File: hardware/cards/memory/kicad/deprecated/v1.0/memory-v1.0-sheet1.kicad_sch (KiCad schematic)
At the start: 5 parts, among them IC10 74*00, IC6 74*04, X1 FABC96R

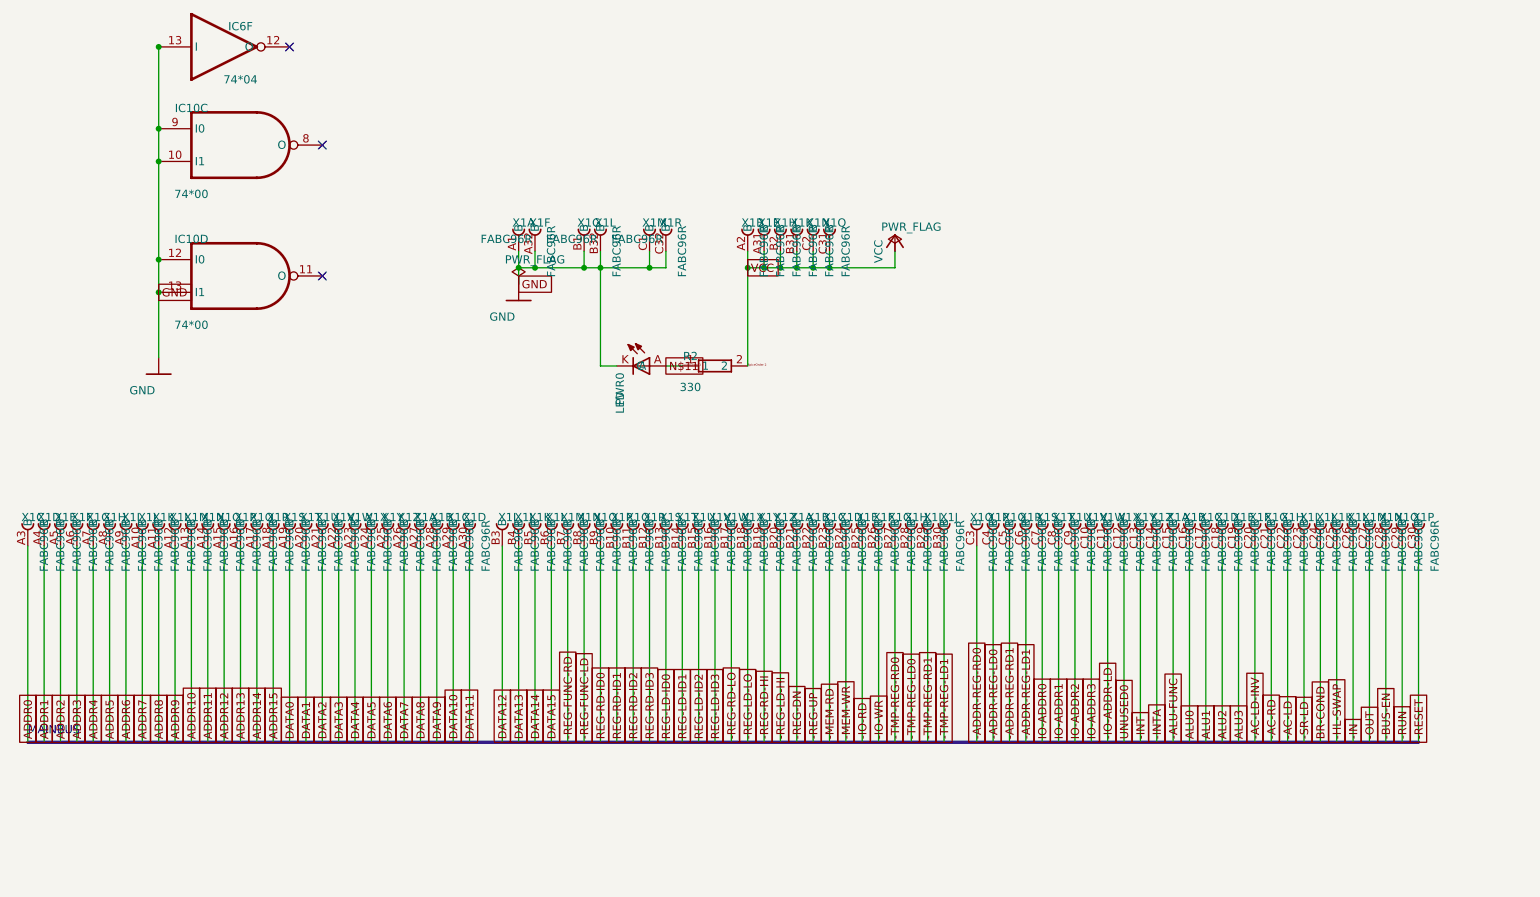
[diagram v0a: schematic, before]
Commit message: fix(kicad): readable converted schematics - overlaps 42,847 -> 3,147, nothing off the frame; CF sheet 0 overlaps
- tools/kicad/sch_overlaps.py: calibrated readability check (text/text, text/body, text/line, off frame/title block)
- eagle_sch_to_kicad.py: fields placed from Eagle's smashed attributes or the symbol's >NAME/>VALUE with Eagle's align,
  size and ratio, readable angles; fields Eagle never shows hidden (FABC96R shows only its pin name); pin numbers hidden
  where every Eagle pin hides them; Eagle-hidden layers dropped (the stray SpiceOrder text); labels on their own wires,
  converter labels only where KiCad needs them; rotate-then-mirror fixed for MR90/MR270 in pin_world/no-connects;
  each sheet on the smallest page that holds it, centred clear of the title block
- finish_board.py: stable footprint-library choice (DRC counts no longer vary run to run)
- all 37 projects regenerated: netlist proofs unchanged (34 MATCH, 2 schematic-only, video Fusion export MISMATCH as
  before); DRC same or better; ERC up (loose wire ends onto graphic buses no longer hidden by labels; explained per README)
- CF card: gate names off the gate bodies, U3 clear of its title, 5.08 mm connector pins; rebuilt: DRC 0/0, proof MATCH
- schematic PDFs regenerated (tools/sch_to_pdf.py, 37/37)

Co-Authored-By: Claude Opus 5.5 <noreply@anthropic.com>
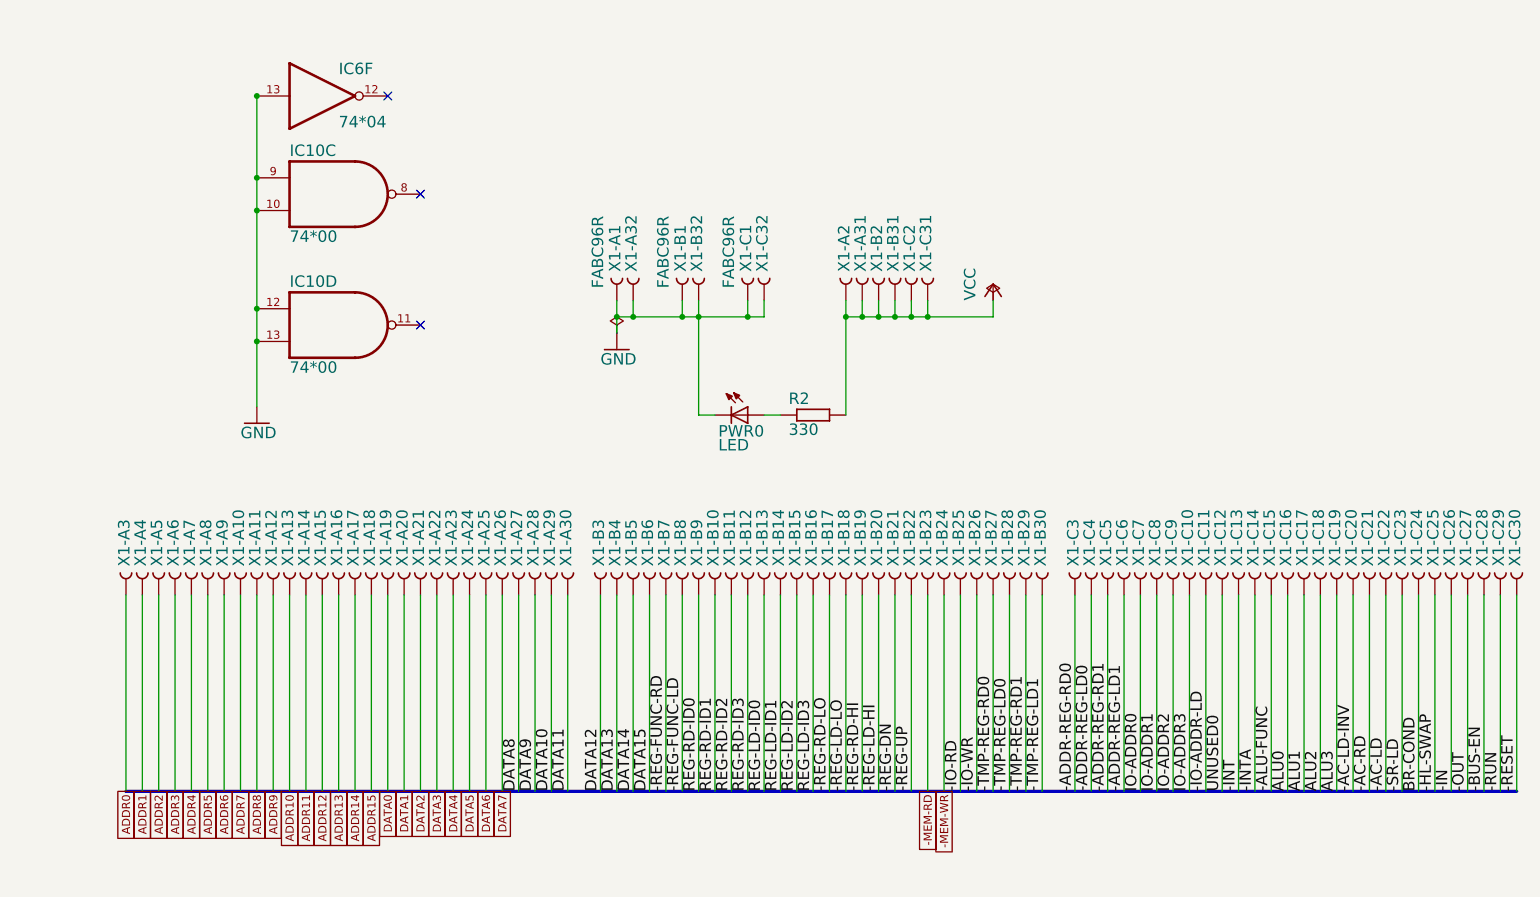
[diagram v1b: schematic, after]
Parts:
- X1: Eagle name (none) -> X1-C29
- X1: Eagle name (none) -> X1-A26
- X1: Eagle name (none) -> X1-C25
- X1: Eagle name (none) -> X1-C16
- X1: Eagle name (none) -> X1-A14
- X1: Eagle name (none) -> X1-A2
- X1: Eagle name (none) -> X1-B24
- X1: Eagle name (none) -> X1-B30
- X1: Eagle name (none) -> X1-C12
- X1: Eagle name (none) -> X1-B13
- X1: Eagle name (none) -> X1-A19
- X1: Eagle name (none) -> X1-A7
- X1: Eagle name (none) -> X1-A27
- X1: Eagle name (none) -> X1-C4
- X1: Eagle name (none) -> X1-B4
- X1: Eagle name (none) -> X1-A10
- X1: Eagle name (none) -> X1-B5
- X1: Eagle name (none) -> X1-B15
- X1: Eagle name (none) -> X1-B10
- X1: Eagle name (none) -> X1-A24
- X1: Eagle name (none) -> X1-B12
- X1: Eagle name (none) -> X1-B32
- X1: Eagle name (none) -> X1-B21
- X1: Eagle name (none) -> X1-B29
- X1: Eagle name (none) -> X1-B8
- X1: Eagle name (none) -> X1-C19
- X1: Eagle name (none) -> X1-B23
- X1: Eagle name (none) -> X1-C20
- X1: Eagle name (none) -> X1-C27
- X1: Eagle name (none) -> X1-C18
- X1: Eagle name (none) -> X1-B11
- X1: Eagle name (none) -> X1-A4
- X1: Eagle name (none) -> X1-A16
- X1: Eagle name (none) -> X1-C11
- X1: Eagle name (none) -> X1-B2
- X1: Eagle name (none) -> X1-C32
- X1: Eagle name (none) -> X1-C1
- X1: Eagle name (none) -> X1-B22
- X1: Eagle name (none) -> X1-C30
- X1: Eagle name (none) -> X1-A8
- X1: Eagle name (none) -> X1-A28
- X1: Eagle name (none) -> X1-C26
- X1: Eagle name (none) -> X1-B3
- X1: Eagle name (none) -> X1-C5
- X1: Eagle name (none) -> X1-A17
- X1: Eagle name (none) -> X1-C6
- X1: Eagle name (none) -> X1-A18
- X1: Eagle name (none) -> X1-A25
- X1: Eagle name (none) -> X1-A12
- X1: Eagle name (none) -> X1-C23
- X1: Eagle name (none) -> X1-A23
- X1: Eagle name (none) -> X1-A21
- X1: Eagle name (none) -> X1-C8
- X1: Eagle name (none) -> X1-C7
- X1: Eagle name (none) -> X1-A1
- X1: Eagle name (none) -> X1-B28
- X1: Eagle name (none) -> X1-B9
- X1: Eagle name (none) -> X1-B1
- X1: Eagle name (none) -> X1-C2
- X1: Eagle name (none) -> X1-B14
- X1: Eagle name (none) -> X1-A11
- X1: Eagle name (none) -> X1-C14
- X1: Eagle name (none) -> X1-A30
- X1: Eagle name (none) -> X1-A32
- X1: Eagle name (none) -> X1-B25
- X1: Eagle name (none) -> X1-B31
- X1: Eagle name (none) -> X1-B26
- X1: Eagle name (none) -> X1-C28
- X1: Eagle name (none) -> X1-A20
- X1: Eagle name (none) -> X1-A3
- X1: Eagle name (none) -> X1-B20
- X1: Eagle name (none) -> X1-B17
- X1: Eagle name (none) -> X1-A9
- X1: Eagle name (none) -> X1-C24
- X1: Eagle name (none) -> X1-C3
- X1: Eagle name (none) -> X1-C31
- X1: Eagle name (none) -> X1-C15
- X1: Eagle name (none) -> X1-B18
- X1: Eagle name (none) -> X1-A22
- X1: Eagle name (none) -> X1-A15
- X1: Eagle name (none) -> X1-A5
- X1: Eagle name (none) -> X1-B7
- X1: Eagle name (none) -> X1-B19
- X1: Eagle name (none) -> X1-A13
- X1: Eagle name (none) -> X1-C21
- X1: Eagle name (none) -> X1-C22
- X1: Eagle name (none) -> X1-B27
- X1: Eagle name (none) -> X1-C10
- X1: Eagle name (none) -> X1-B6
- X1: Eagle name (none) -> X1-A6
- X1: Eagle name (none) -> X1-C17
- X1: Eagle name (none) -> X1-A31
- X1: Eagle name (none) -> X1-A29
- X1: Eagle name (none) -> X1-B16
- X1: Eagle name (none) -> X1-C9
- X1: Eagle name (none) -> X1-C13
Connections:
- net N$11: no longer names the net of PWR0.A, R2.1
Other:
- note removed: "MAINBUS"
